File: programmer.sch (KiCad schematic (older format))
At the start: 38 parts

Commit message: Finish LED branches on programmer sheet
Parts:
- removed U? (x2): 74AHC1G04, symbol 74xGxx:74AHC1G04
- added C?: 100n, symbol Device:C
- added D?: USBPWR, symbol Device:LED
- added D?: USBSUSPEND, symbol Device:LED
- added R? (x2): R, symbol Device:R
- added U? (x5): 74HC14, symbol 74xx:74HC14
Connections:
- net +3V3: now also U?.8 (VCC), C?.1, U?.14 (VCC)
- net at R?.2, U?.P8 (~INIT~_0): now also U?.3
- net at U?.P9 (DONE_0): now also U?.1
- net at U?.36 (~SUSPEND): now also U?.11
- net at U?.60 (~PWREN): now also U?.5
- net at D?.2 (A): now also U?.4
- net at D?.2 (A): now also U?.2
- net GND renamed GNDD
- net GNDD: now also C?.2, R?.2, R?.2, U?.7 (GND)
- new net: D?.1 (K), R?.1 (x2)
- new net: D?.2 (A), U?.6
- new net: D?.2 (A), U?.10
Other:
- moved on the sheet: C?, D?, R?

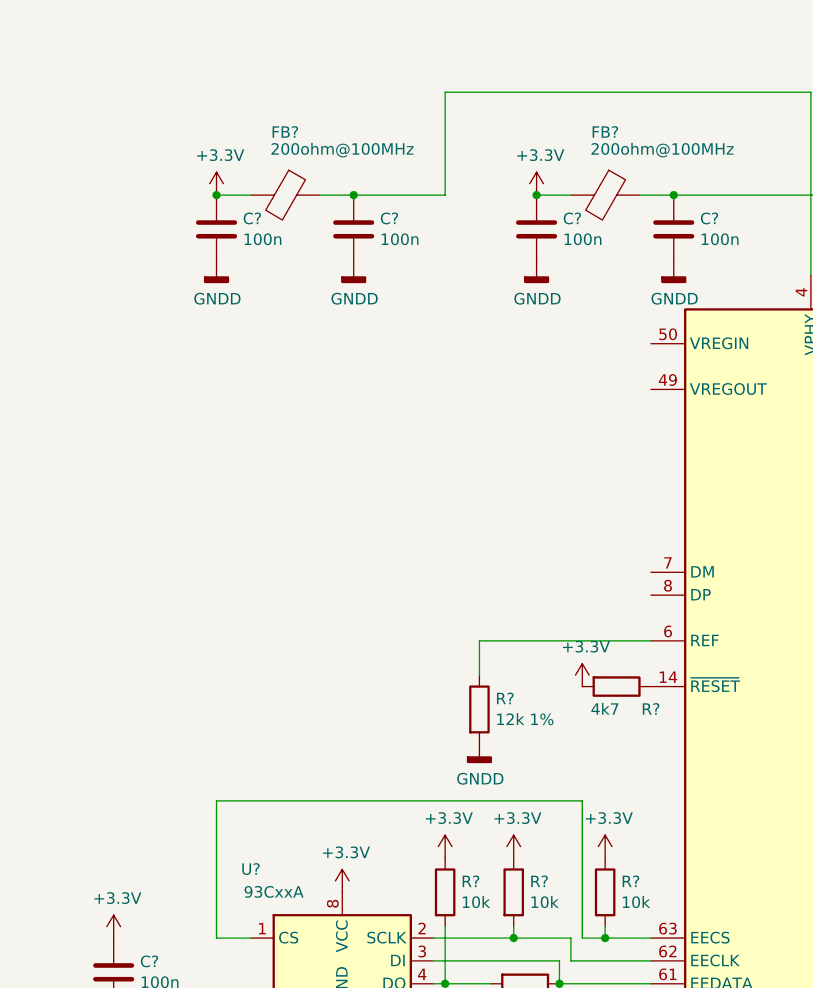
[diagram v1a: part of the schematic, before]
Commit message: Add USB connector
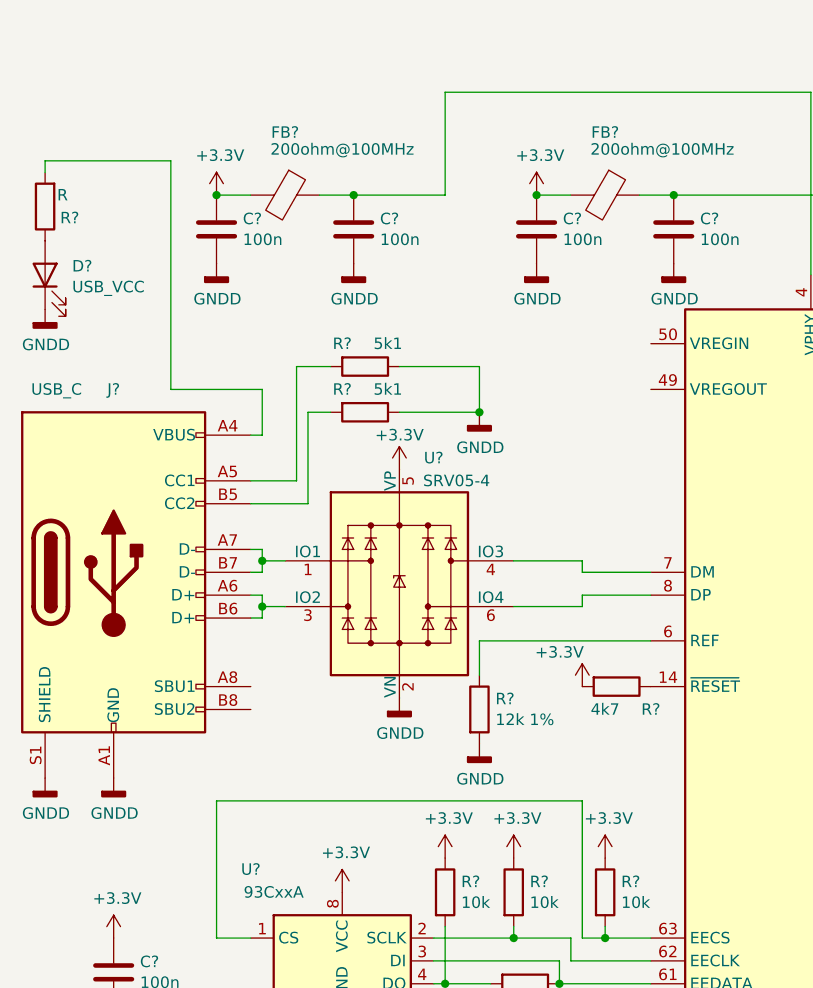
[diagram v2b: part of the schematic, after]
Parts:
- added D?: USB_VCC, symbol Device:LED
- added J?: USB_C, symbol Connector:USB_C_Receptacle_USB2.0
- added R? (x2): 5k1, symbol Device:R
- added R?: R, symbol Device:R
- added U?: SRV05-4, Package_TO_SOT_SMD:SOT-23-6, symbol Power_Protection:SRV05-4
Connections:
- net +3V3: now also U?.5 (VP)
- net GNDD: now also D?.1 (K), J?.A1 (GND), J?.A12 (GND), J?.B1 (GND), J?.B12 (GND), J?.S1 (SHIELD), R?.1, R?.1, U?.2 (VN)
- net at U?.7 (DM): now also U?.4 (IO3)
- net at U?.8 (DP): now also U?.6 (IO4)
- new net: J?.A7 (D-), J?.B7 (D-), U?.1 (IO1)
- new net: J?.A6 (D+), J?.B6 (D+), U?.3 (IO2)
- new net: J?.A4 (VBUS), J?.A9 (VBUS), J?.B4 (VBUS), J?.B9 (VBUS), R?.2
- new net: J?.A5 (CC1), R?.2
- new net: J?.B5 (CC2), R?.2
- new net: D?.2 (A), R?.1
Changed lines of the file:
@@
 P 2950 3400
 F 0 "#PWR?" H 2950 3250 50  0001 C CNN
-F 1 "+3.3V" H 2965 3573 50  0000 C CNN
+F 1 "+3.3V" H 2850 3550 50  0000 C CNN
 F 2 "" H 2950 3400 50  0001 C CNN
 F 3 "" H 2950 3400 50  0001 C CNN
@@
 Wire Wire Line
 	9650 2250 9900 2250
+$Comp
+L Power_Protection:SRV05-4 U?
+U 1 1 609C95A3
+P 2150 2950
+F 0 "U?" H 2300 3500 50  0000 C CNN
+F 1 "SRV05-4" H 2400 3400 50  0000 C CNN
+F 2 "Package_TO_SOT_SMD:SOT-23-6" H 2850 2500 50  0001 C CNN
+F 3 "http://www.onsemi.com/pub/Collateral/SRV05-4-D.PDF" H 2150 2950 50  0001 C CNN
+	1    2150 2950
+	1    0    0    -1
+$EndComp
+Wire Wire Line
+	3250 2900 2950 2900
+Wire Wire Line
+	2950 2900 2950 2850
+Wire Wire Line
+	2950 2850 2650 2850
+Wire Wire Line
+	3250 3000 2950 3000
+Wire Wire Line
+	2950 3000 2950 3050
+Wire Wire Line
+	2950 3050 2650 3050
+$Comp
+L power:GNDD #PWR?
+U 1 1 609D7882
+P 2150 3450
+F 0 "#PWR?" H 2150 3200 50  0001 C CNN
+F 1 "GNDD" H 2154 3295 50  0000 C CNN
+F 2 "" H 2150 3450 50  0001 C CNN
+F 3 "" H 2150 3450 50  0001 C CNN
+	1    2150 3450
+	1    0    0    -1
+$EndComp
+$Comp
+L power:+3.3V #PWR?
+U 1 1 609D7B90
+P 2150 2450
+F 0 "#PWR?" H 2150 2300 50  0001 C CNN
+F 1 "+3.3V" H 2150 2600 50  0000 C CNN
+F 2 "" H 2150 2450 50  0001 C CNN
+F 3 "" H 2150 2450 50  0001 C CNN
+	1    2150 2450
+	1    0    0    -1
+$EndComp
+$Comp
+L Connector:USB_C_Receptacle_USB2.0 J?
+U 1 1 609DADDC
+P 900 2900
+F 0 "J?" H 900 3700 50  0000 C CNN
+F 1 "USB_C" H 650 3700 50  0000 C CNN
+F 2 "" H 1050 2900 50  0001 C CNN
+F 3 "https://www.usb.org/sites/default/files/documents/usb_type-c.zip" H 1050 2900 50  0001 C CNN
+	1    900  2900
+	1    0    0    -1
+$EndComp
+Wire Wire Line
+	1500 2800 1550 2800
+Wire Wire Line
+	1550 2800 1550 2850
+Wire Wire Line
+	1550 2850 1650 2850
+Wire Wire Line
+	1500 2900 1550 2900
+Wire Wire Line
+	1550 2900 1550 2850
+Connection ~ 1550 2850
+Wire Wire Line
+	1500 3000 1550 3000
+Wire Wire Line
+	1550 3000 1550 3050
+Wire Wire Line
+	1550 3050 1650 3050
+Wire Wire Line
+	1500 3100 1550 3100
+Wire Wire Line
+	1550 3100 1550 3050
+Connection ~ 1550 3050
+$Comp
+L power:GNDD #PWR?
+U 1 1 609F6D45
+P 900 3800
+F 0 "#PWR?" H 900 3550 50  0001 C CNN
+F 1 "GNDD" H 904 3645 50  0000 C CNN
+F 2 "" H 900 3800 50  0001 C CNN
+F 3 "" H 900 3800 50  0001 C CNN
+	1    900  3800
+	1    0    0    -1
+$EndComp
+$Comp
+L power:GNDD #PWR?
+U 1 1 609F799C
+P 600 3800
+F 0 "#PWR?" H 600 3550 50  0001 C CNN
+F 1 "GNDD" H 604 3645 50  0000 C CNN
+F 2 "" H 600 3800 50  0001 C CNN
+F 3 "" H 600 3800 50  0001 C CNN
+	1    600  3800
+	1    0    0    -1
+$EndComp
+$Comp
+L Device:R R?
+U 1 1 609F89F6
+P 2000 2000
+F 0 "R?" V 1900 1900 50  0000 C CNN
+F 1 "5k1" V 1900 2100 50  0000 C CNN
+F 2 "" V 1930 2000 50  0001 C CNN
+F 3 "~" H 2000 2000 50  0001 C CNN
+	1    2000 2000
+	0    1    1    0
+$EndComp
+$Comp
+L Device:R R?
+U 1 1 609F906D
+P 2000 2200
+F 0 "R?" V 1900 2100 50  0000 C CNN
+F 1 "5k1" V 1900 2300 50  0000 C CNN
+F 2 "" V 1930 2200 50  0001 C CNN
+F 3 "~" H 2000 2200 50  0001 C CNN
+	1    2000 2200
+	0    1    1    0
+$EndComp
+$Comp
+L power:GNDD #PWR?
+U 1 1 609FA29C
+P 2500 2200
+F 0 "#PWR?" H 2500 1950 50  0001 C CNN
+F 1 "GNDD" H 2504 2045 50  0000 C CNN
+F 2 "" H 2500 2200 50  0001 C CNN
+F 3 "" H 2500 2200 50  0001 C CNN
+	1    2500 2200
+	1    0    0    -1
+$EndComp
+Wire Wire Line
+	2500 2200 2150 2200
+Wire Wire Line
+	2150 2000 2500 2000
+Wire Wire Line
+	2500 2000 2500 2200
+Connection ~ 2500 2200
+Wire Wire Line
+	1700 2000 1700 2500
+Wire Wire Line
+	1700 2500 1500 2500
+Wire Wire Line
+	1700 2000 1850 2000
+Wire Wire Line
+	1500 2600 1750 2600
+Wire Wire Line
+	1750 2600 1750 2200
+Wire Wire Line
+	1750 2200 1850 2200
+$Comp
+L Device:R R?
+U 1 1 60A1D461
+P 600 1300
+F 0 "R?" H 450 1350 50  0000 L CNN
+F 1 "R" H 500 1250 50  0000 L CNN
+F 2 "" V 530 1300 50  0001 C CNN
+F 3 "~" H 600 1300 50  0001 C CNN
+	1    600  1300
+	-1   0    0    1
+$EndComp
+$Comp
+L Device:LED D?
+U 1 1 60A1E03B
+P 600 1600
+F 0 "D?" V 639 1482 50  0000 R CNN
+F 1 "USB_VCC" V 548 1482 50  0000 R CNN
+F 2 "" H 600 1600 50  0001 C CNN
+F 3 "~" H 600 1600 50  0001 C CNN
+	1    600  1600
+	0    -1   -1   0
+$EndComp
+$Comp
+L power:GNDD #PWR?
+U 1 1 60A4614E
+P 600 1750
+F 0 "#PWR?" H 600 1500 50  0001 C CNN
+F 1 "GNDD" H 604 1595 50  0000 C CNN
+F 2 "" H 600 1750 50  0001 C CNN
+F 3 "" H 600 1750 50  0001 C CNN
+	1    600  1750
+	1    0    0    -1
+$EndComp
+Wire Wire Line
+	600  1150 600  1100
+Wire Wire Line
+	600  1100 1150 1100
+Wire Wire Line
+	1150 1100 1150 2100
+Wire Wire Line
+	1150 2100 1550 2100
+Wire Wire Line
+	1550 2100 1550 2300
+Wire Wire Line
+	1550 2300 1500 2300
 Wire Bus Line
 	6100 3700 6100 4200

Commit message: Fix power pins
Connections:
- net +3V3: now also U?.N6 (VCCO_0), U?.N8 (VCCO_0)
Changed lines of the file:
@@
 Wire Wire Line
 	1550 2300 1500 2300
+$Comp
+L power:+3.3V #PWR?
+U 1 1 609FACC9
+P 6900 1400
+F 0 "#PWR?" H 6900 1250 50  0001 C CNN
+F 1 "+3.3V" H 6915 1573 50  0000 C CNN
+F 2 "" H 6900 1400 50  0001 C CNN
+F 3 "" H 6900 1400 50  0001 C CNN
+	1    6900 1400
+	1    0    0    -1
+$EndComp
+Wire Wire Line
+	7000 1550 6900 1550
+Wire Wire Line
+	6900 1550 6900 1450
+Wire Wire Line
+	7000 1450 6900 1450
 Wire Bus Line
 	6100 3700 6100 4200
@@
 Wire Bus Line
 	6100 4300 6100 5500
+Connection ~ 6900 1450
+Wire Wire Line
+	6900 1450 6900 1400
 $EndSCHEMATC
